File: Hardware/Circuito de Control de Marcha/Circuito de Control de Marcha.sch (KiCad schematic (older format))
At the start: 42 parts, among them Q1 IRF9540N, Q1A1 2N2219, Q2 IRF540N, Q2A1 2N2219, Q3 IRF9540N, Q3A1 2N2219, Q4 IRF540N, Q4A1 2N2219, Q5 IRF9540N, Q5A1 2N2219, Q6 IRF540N, Q6A1 2N2219, Q7 IRF9540N, Q7A1 2N2219, Q8 IRF540N, Q8A1 2N2219, U1 ULN2003

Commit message: Correxion en el control de marcha
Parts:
- removed uC_Direccion1: Screw_Terminal_01x05, Connector_Molex:Molex_KK-254_AE-6410-05A_1x05_P2.54mm_Vertical, symbol Connector:Screw_Terminal_01x05
- added uCDireccion1: Screw_Terminal_01x04, Connector_Molex:Molex_KK-254_AE-6410-04A_1x04_P2.54mm_Vertical, symbol Connector:Screw_Terminal_01x04
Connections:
- wire segments 123 -> 120
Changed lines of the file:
@@
 Wire Wire Line
 	3350 5550 4450 5550
-$Comp
-L Connector:Screw_Terminal_01x05 uC_Direccion1
-U 1 1 5E9D6D91
-P 1050 5450
-F 0 "uC_Direccion1" H 968 5775 50  0000 C CNN
-F 1 "Screw_Terminal_01x05" H 968 5776 50  0001 C CNN
-F 2 "Connector_Molex:Molex_KK-254_AE-6410-05A_1x05_P2.54mm_Vertical" H 1050 5450 50  0001 C CNN
-F 3 "~" H 1050 5450 50  0001 C CNN
-	1    1050 5450
-	-1   0    0    -1
-$EndComp
-Wire Wire Line
-	1250 5650 1450 5650
-Wire Wire Line
-	1450 5650 1450 6050
-Wire Wire Line
-	1450 6050 2950 6050
 Connection ~ 2950 6050
 $Comp
@@
 Wire Wire Line
 	5050 6050 2950 6050
+$Comp
+L Connector:Screw_Terminal_01x04 uCDireccion1
+U 1 1 5EFAC944
+P 1050 5450
+F 0 "uCDireccion1" H 968 5025 50  0000 C CNN
+F 1 "Screw_Terminal_01x04" H 968 5116 50  0000 C CNN
+F 2 "Connector_Molex:Molex_KK-254_AE-6410-04A_1x04_P2.54mm_Vertical" H 1050 5450 50  0001 C CNN
+F 3 "~" H 1050 5450 50  0001 C CNN
+	1    1050 5450
+	-1   0    0    1
+$EndComp
 $EndSCHEMATC

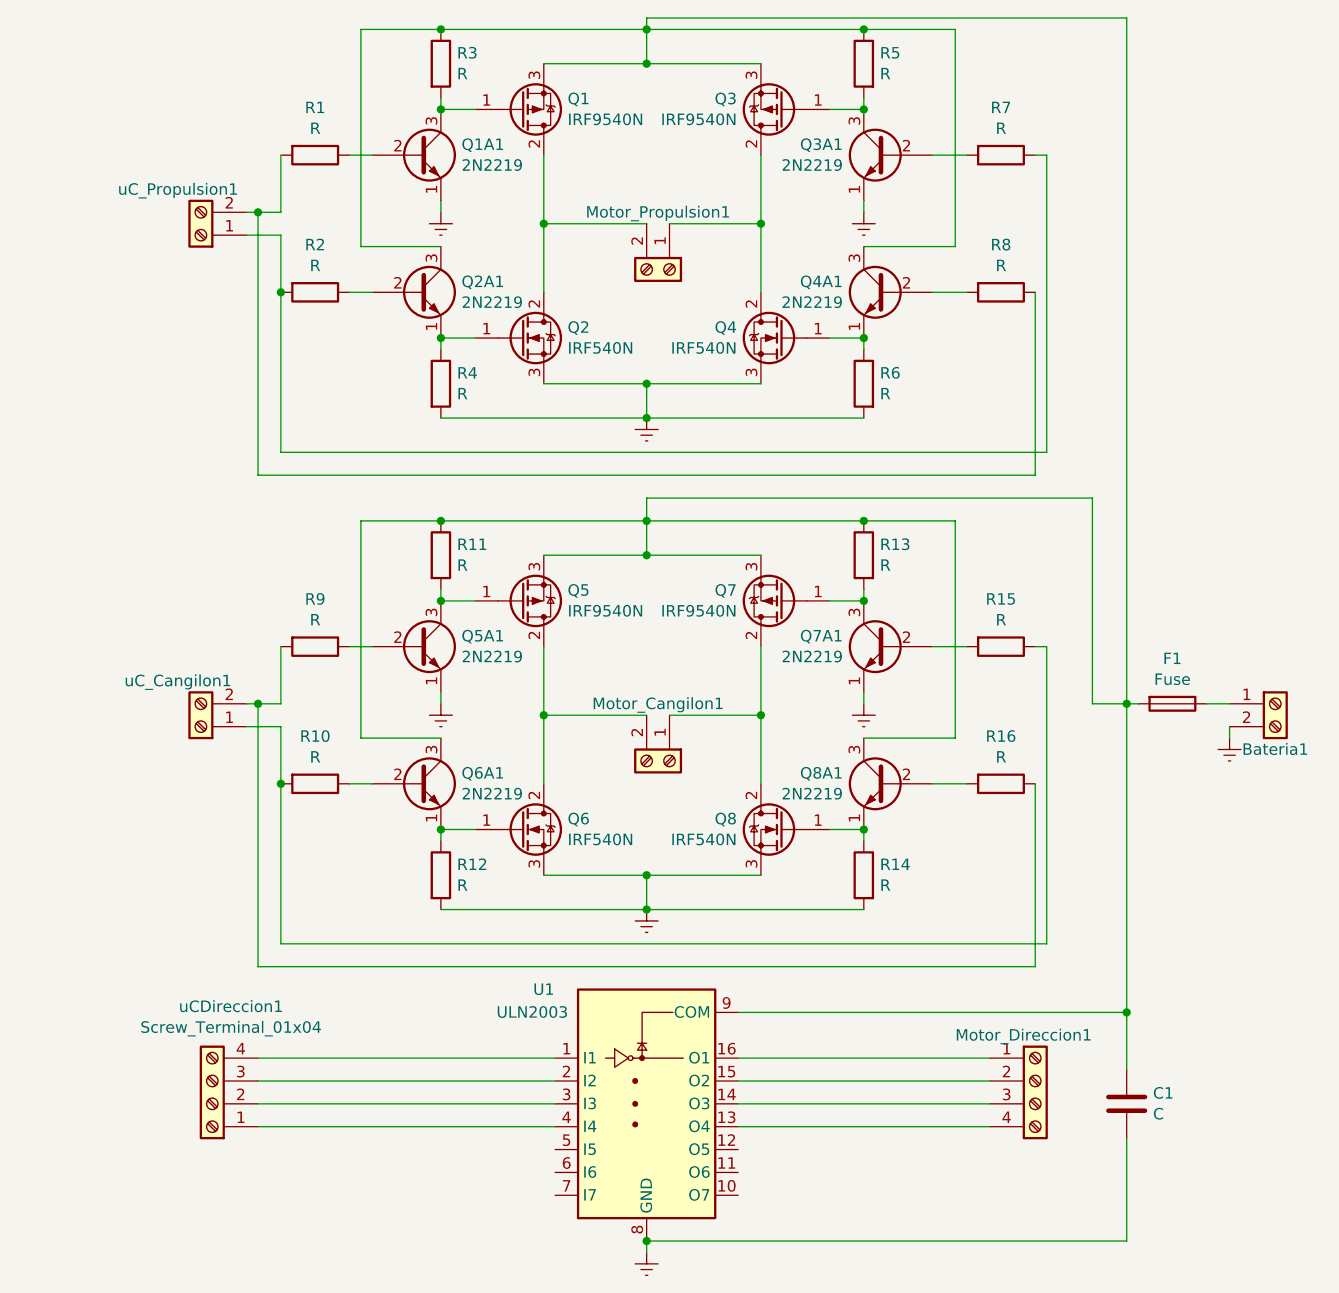
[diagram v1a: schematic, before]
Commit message: Esquematico CCM
Puse los optoacopladores en el controlador de marcha
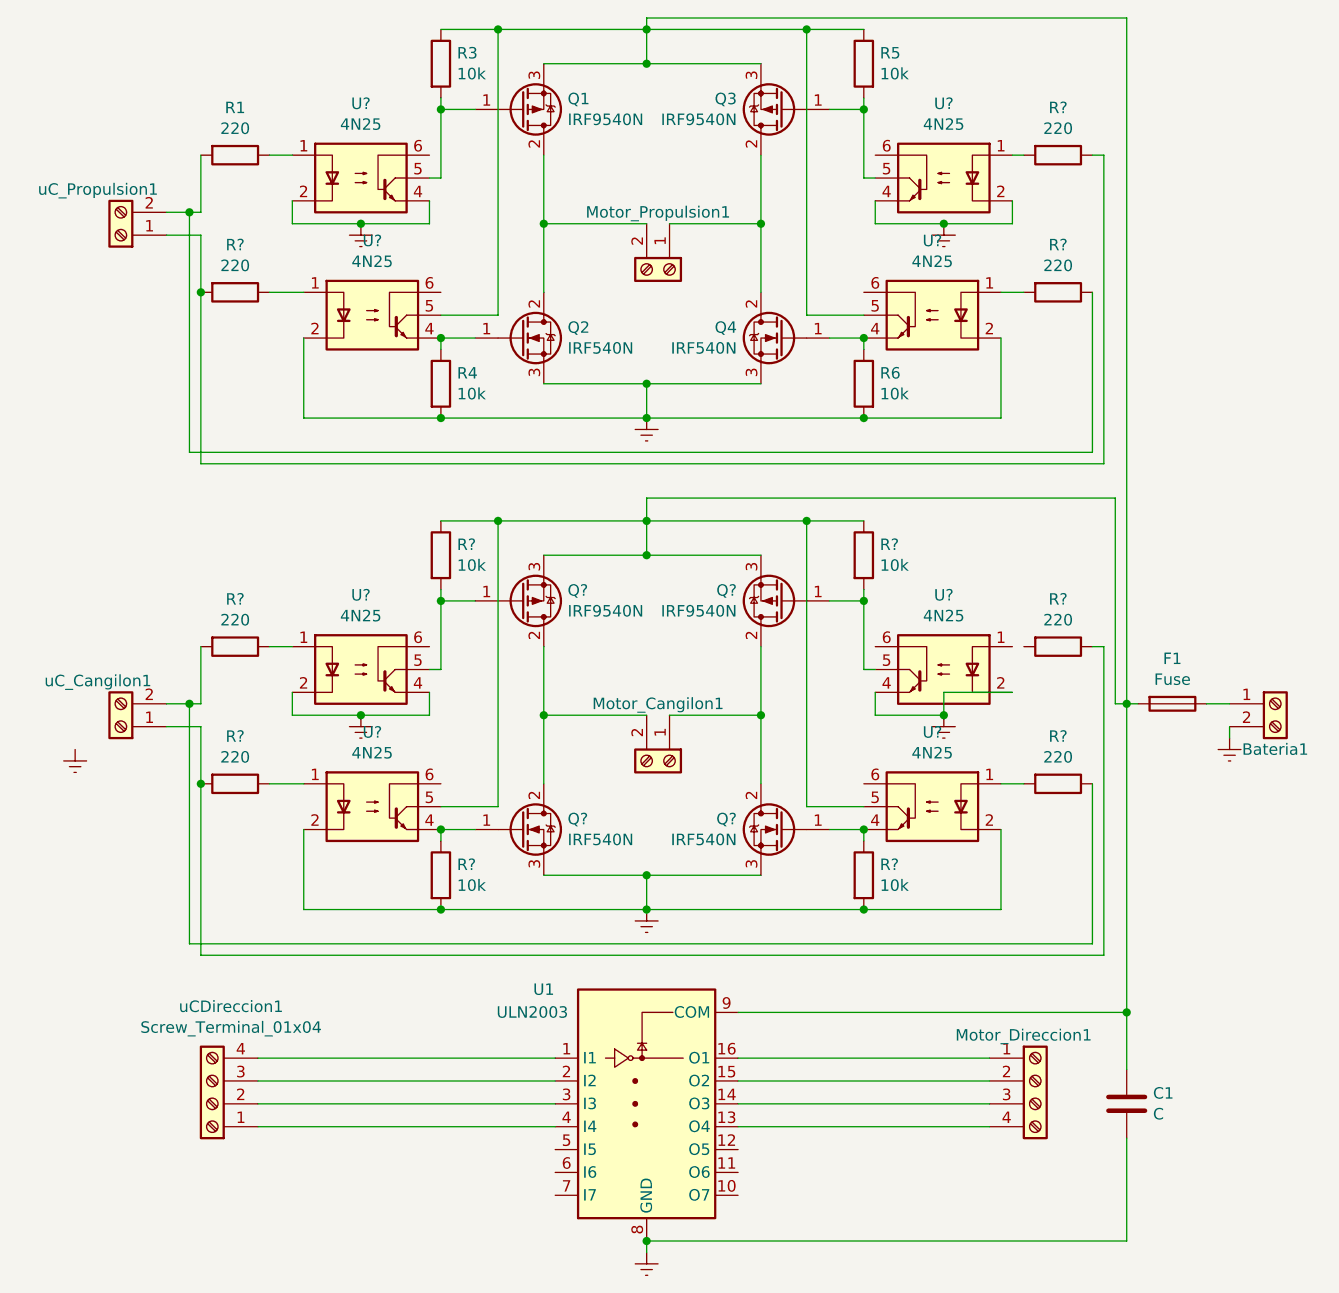
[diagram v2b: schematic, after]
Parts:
- removed Q1A1, Q2A1, Q3A1, Q4A1, Q5A1, Q6A1, Q7A1, Q8A1: 2N2219, Package_TO_SOT_THT:TO-92L_Inline_Wide, symbol Transistor_BJT:2N2219
- removed Q5, Q7: IRF9540N, Package_TO_SOT_THT:TO-220-3_Vertical, symbol Transistor_FET:IRF9540N
- removed Q6, Q8: IRF540N, Package_TO_SOT_THT:TO-220-3_Vertical, symbol Transistor_FET:IRF540N
- removed R10, R11, R12, R13, R14, R15, R16, R2, R7, R8, R9: R, Resistor_THT:R_Axial_DIN0204_L3.6mm_D1.6mm_P7.62mm_Horizontal, symbol Device:R
- added Q? (x2): IRF9540N, Package_TO_SOT_THT:TO-220-3_Vertical, symbol Transistor_FET:IRF9540N
- added Q? (x2): IRF540N, Package_TO_SOT_THT:TO-220-3_Vertical, symbol Transistor_FET:IRF540N
- added R? (x7): 220, Resistor_THT:R_Axial_DIN0204_L3.6mm_D1.6mm_P7.62mm_Horizontal, symbol Device:R
- added R? (x4): 10k, Resistor_THT:R_Axial_DIN0204_L3.6mm_D1.6mm_P7.62mm_Horizontal, symbol Device:R
- added U? (x8): 4N25, Package_DIP:DIP-6_W7.62mm, symbol Isolator:4N25
- R1: value R -> 220
- R3, R4, R5, R6: value R -> 10k
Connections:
- net Earth: now also Q?.3 (S), Q?.3 (S), R?.2, R?.2, U?.2, U?.2, U?.2, U?.2, U?.2, U?.2, U?.2, U?.2, U?.4, U?.4, U?.4, U?.4
- net at uC_Propulsion1.1 (Pin_1): now also R?.1, R?.2
- net at R1.2, uC_Propulsion1.2 (Pin_2): now also R?.1
- net at C1.1, F1.2, Q1.3 (S)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: now also Q?.3 (S), Q?.3 (S), R?.1, R?.1, U?.5, U?.5, U?.5, U?.5
- net at Q1.1 (G), R3.2: now also U?.5
- net at Q2.1 (G), R4.1: now also U?.4
- net at R1.1: now also U?.1
- net at Q3.1 (G), R5.2: now also U?.5
- net at Q4.1 (G), R6.1: now also U?.4
- net at uC_Cangilon1.1 (Pin_1): now also R?.1, R?.2
- net at uC_Cangilon1.2 (Pin_2): now also R?.1, R?.2
- net at Motor_Cangilon1.2 (Pin_2): now also Q?.2 (D), Q?.2 (D)
- net at Motor_Cangilon1.1 (Pin_1): now also Q?.2 (D), Q?.2 (D)
- new net: R?.1, U?.1 (x3)
- new net: R?.2, U?.1 (x3)
- new net: Q?.1 (G), R?.2, U?.5 (x2)
- new net: Q?.1 (G), R?.1, U?.4 (x2)
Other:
- moved on the sheet: R1, uC_Cangilon1, uC_Propulsion1

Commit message: PCB control de marcha
Intente hacer el PCB pero me queda una conexion de los púentes H
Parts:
- gave numbers to parts that had none: 23
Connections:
- net at U9.1: now also R15.2
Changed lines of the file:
@@
 $EndComp
 $Comp
-L Isolator:4N25 U?
+L Isolator:4N25 U2
 U 1 1 5F002069
 P 1700 1400
-F 0 "U?" H 1700 1725 50  0000 C CNN
+F 0 "U2" H 1700 1725 50  0000 C CNN
 F 1 "4N25" H 1700 1634 50  0000 C CNN
 F 2 "Package_DIP:DIP-6_W7.62mm" H 1500 1200 50  0001 L CIN
@@
 Connection ~ 1700 1600
 $Comp
-L Isolator:4N25 U?
+L Isolator:4N25 U4
 U 1 1 5F020A68
 P 1750 2000
-F 0 "U?" H 1750 2325 50  0000 C CNN
+F 0 "U4" H 1750 2325 50  0000 C CNN
 F 1 "4N25" H 1750 2234 50  0000 C CNN
 F 2 "Package_DIP:DIP-6_W7.62mm" H 1550 1800 50  0001 L CIN
@@
 Connection ~ 2050 2450
 $Comp
-L Isolator:4N25 U?
+L Isolator:4N25 U6
 U 1 1 5F02FF87
 P 4200 2000
-F 0 "U?" H 4200 2325 50  0000 C CNN
+F 0 "U6" H 4200 2325 50  0000 C CNN
 F 1 "4N25" H 4200 2234 50  0000 C CNN
 F 2 "Package_DIP:DIP-6_W7.62mm" H 4000 1800 50  0001 L CIN
@@
 Connection ~ 3900 2100
 $Comp
-L Isolator:4N25 U?
+L Isolator:4N25 U8
 U 1 1 5F033177
 P 4250 1400
-F 0 "U?" H 4250 1725 50  0000 C CNN
+F 0 "U8" H 4250 1725 50  0000 C CNN
 F 1 "4N25" H 4250 1634 50  0000 C CNN
 F 2 "Package_DIP:DIP-6_W7.62mm" H 4050 1200 50  0001 L CIN
@@
 	4950 2650 1000 2650
 $Comp
-L Transistor_FET:IRF9540N Q?
+L Transistor_FET:IRF9540N Q5
 U 1 1 5F05B32E
 P 2400 3250
-F 0 "Q?" H 2604 3204 50  0000 L CNN
+F 0 "Q5" H 2604 3204 50  0000 L CNN
 F 1 "IRF9540N" H 2604 3295 50  0000 L CNN
 F 2 "Package_TO_SOT_THT:TO-220-3_Vertical" H 2600 3175 50  0001 L CIN
@@
 $EndComp
 $Comp
-L Transistor_FET:IRF9540N Q?
+L Transistor_FET:IRF9540N Q7
 U 1 1 5F05BBDD
 P 3550 3250
-F 0 "Q?" H 3755 3204 50  0000 L CNN
+F 0 "Q7" H 3755 3204 50  0000 L CNN
 F 1 "IRF9540N" H 3755 3295 50  0000 L CNN
 F 2 "Package_TO_SOT_THT:TO-220-3_Vertical" H 3750 3175 50  0001 L CIN
@@
 $EndComp
 $Comp
-L Transistor_FET:IRF540N Q?
+L Transistor_FET:IRF540N Q6
 U 1 1 5F05C27A
 P 2400 4250
-F 0 "Q?" H 2604 4296 50  0000 L CNN
+F 0 "Q6" H 2604 4296 50  0000 L CNN
 F 1 "IRF540N" H 2604 4205 50  0000 L CNN
 F 2 "Package_TO_SOT_THT:TO-220-3_Vertical" H 2650 4175 50  0001 L CIN
@@
 $EndComp
 $Comp
-L Transistor_FET:IRF540N Q?
+L Transistor_FET:IRF540N Q8
 U 1 1 5F05CF57
 P 3550 4250
-F 0 "Q?" H 3755 4296 50  0000 L CNN
+F 0 "Q8" H 3755 4296 50  0000 L CNN
 F 1 "IRF540N" H 3755 4205 50  0000 L CNN
 F 2 "Package_TO_SOT_THT:TO-220-3_Vertical" H 3800 4175 50  0001 L CIN
@@
 	1000 1650 1000 1900
 $Comp
-L Device:R R?
+L Device:R R2
 U 1 1 5F063F20
 P 1150 1900
-F 0 "R?" V 943 1900 50  0000 C CNN
+F 0 "R2" V 943 1900 50  0000 C CNN
 F 1 "220" V 1034 1900 50  0000 C CNN
 F 2 "Resistor_THT:R_Axial_DIN0204_L3.6mm_D1.6mm_P7.62mm_Horizontal" V 1080 1900 50  0001 C CNN
@@
 	1000 1900 1000 2650
 $Comp
-L Device:R R?
+L Device:R R14
 U 1 1 5F0641E7
 P 4750 1900
-F 0 "R?" V 4543 1900 50  0000 C CNN
+F 0 "R14" V 4543 1900 50  0000 C CNN
 F 1 "220" V 4634 1900 50  0000 C CNN
 F 2 "Resistor_THT:R_Axial_DIN0204_L3.6mm_D1.6mm_P7.62mm_Horizontal" V 4680 1900 50  0001 C CNN
@@
 $EndComp
 $Comp
-L Device:R R?
+L Device:R R13
 U 1 1 5F0646E3
 P 4750 1300
-F 0 "R?" V 4543 1300 50  0000 C CNN
+F 0 "R13" V 4543 1300 50  0000 C CNN
 F 1 "220" V 4634 1300 50  0000 C CNN
 F 2 "Resistor_THT:R_Axial_DIN0204_L3.6mm_D1.6mm_P7.62mm_Horizontal" V 4680 1300 50  0001 C CNN
@@
 	850  3700 950  3700
 $Comp
-L Isolator:4N25 U?
+L Isolator:4N25 U5
 U 1 1 5F06CB3C
 P 1750 4150
-F 0 "U?" H 1750 4475 50  0000 C CNN
+F 0 "U5" H 1750 4475 50  0000 C CNN
 F 1 "4N25" H 1750 4384 50  0000 C CNN
 F 2 "Package_DIP:DIP-6_W7.62mm" H 1550 3950 50  0001 L CIN
@@
 Connection ~ 2050 4250
 $Comp
-L Isolator:4N25 U?
+L Isolator:4N25 U3
 U 1 1 5F0726D9
 P 1700 3550
-F 0 "U?" H 1700 3875 50  0000 C CNN
+F 0 "U3" H 1700 3875 50  0000 C CNN
 F 1 "4N25" H 1700 3784 50  0000 C CNN
 F 2 "Package_DIP:DIP-6_W7.62mm" H 1500 3350 50  0001 L CIN
@@
 $EndComp
 $Comp
-L Isolator:4N25 U?
+L Isolator:4N25 U7
 U 1 1 5F0735D6
 P 4200 4150
-F 0 "U?" H 4200 4475 50  0000 C CNN
+F 0 "U7" H 4200 4475 50  0000 C CNN
 F 1 "4N25" H 4200 4384 50  0000 C CNN
 F 2 "Package_DIP:DIP-6_W7.62mm" H 4000 3950 50  0001 L CIN
@@
 Connection ~ 3900 4250
 $Comp
-L Isolator:4N25 U?
+L Isolator:4N25 U9
 U 1 1 5F07448D
 P 4250 3550
-F 0 "U?" H 4250 3875 50  0000 C CNN
+F 0 "U9" H 4250 3875 50  0000 C CNN
 F 1 "4N25" H 4250 3784 50  0000 C CNN
 F 2 "Package_DIP:DIP-6_W7.62mm" H 4050 3350 50  0001 L CIN
@@
 $EndComp
 $Comp
-L power:Earth #PWR?
+L power:Earth #PWR0105
 U 1 1 5F075575
 P 4250 3750
-F 0 "#PWR?" H 4250 3500 50  0001 C CNN
+F 0 "#PWR0105" H 4250 3500 50  0001 C CNN
 F 1 "Earth" H 4250 3600 50  0001 C CNN
 F 2 "" H 4250 3750 50  0001 C CNN
@@
 $EndComp
 $Comp
-L Device:R R?
+L Device:R R16
 U 1 1 5F07592F
 P 4750 4050
-F 0 "R?" V 4543 4050 50  0000 C CNN
+F 0 "R16" V 4543 4050 50  0000 C CNN
 F 1 "220" V 4634 4050 50  0000 C CNN
 F 2 "Resistor_THT:R_Axial_DIN0204_L3.6mm_D1.6mm_P7.62mm_Horizontal" V 4680 4050 50  0001 C CNN
@@
 $EndComp
 $Comp
-L Device:R R?
+L Device:R R15
 U 1 1 5F075D82
 P 4750 3450
-F 0 "R?" V 4543 3450 50  0000 C CNN
+F 0 "R15" V 4543 3450 50  0000 C CNN
 F 1 "220" V 4634 3450 50  0000 C CNN
 F 2 "Resistor_THT:R_Axial_DIN0204_L3.6mm_D1.6mm_P7.62mm_Horizontal" V 4680 3450 50  0001 C CNN
@@
 	2950 2800 5000 2800
 $Comp
-L Device:R R?
+L Device:R R7
 U 1 1 5F07AAF0
 P 1150 3450
-F 0 "R?" V 943 3450 50  0000 C CNN
+F 0 "R7" V 943 3450 50  0000 C CNN
 F 1 "220" V 1034 3450 50  0000 C CNN
 F 2 "Resistor_THT:R_Axial_DIN0204_L3.6mm_D1.6mm_P7.62mm_Horizontal" V 1080 3450 50  0001 C CNN
@@
 $EndComp
 $Comp
-L Device:R R?
+L Device:R R8
 U 1 1 5F07B007
 P 1150 4050
-F 0 "R?" V 943 4050 50  0000 C CNN
+F 0 "R8" V 943 4050 50  0000 C CNN
 F 1 "220" V 1034 4050 50  0000 C CNN
 F 2 "Resistor_THT:R_Axial_DIN0204_L3.6mm_D1.6mm_P7.62mm_Horizontal" V 1080 4050 50  0001 C CNN
@@
 	1300 4050 1450 4050
 $Comp
-L power:Earth #PWR?
+L power:Earth #PWR0109
 U 1 1 5F083A08
 P 1700 3750
-F 0 "#PWR?" H 1700 3500 50  0001 C CNN
+F 0 "#PWR0109" H 1700 3500 50  0001 C CNN
 F 1 "Earth" H 1700 3600 50  0001 C CNN
 F 2 "" H 1700 3750 50  0001 C CNN
@@
 	2950 4600 3900 4600
 $Comp
-L Device:R R?
+L Device:R R9
 U 1 1 5F0CA0D4
 P 2050 3050
-F 0 "R?" H 2120 3096 50  0000 L CNN
+F 0 "R9" H 2120 3096 50  0000 L CNN
 F 1 "10k" H 2120 3005 50  0000 L CNN
 F 2 "Resistor_THT:R_Axial_DIN0204_L3.6mm_D1.6mm_P7.62mm_Horizontal" V 1980 3050 50  0001 C CNN
@@
 $EndComp
 $Comp
-L Device:R R?
+L Device:R R10
 U 1 1 5F0CA4D1
 P 2050 4450
-F 0 "R?" H 2120 4496 50  0000 L CNN
+F 0 "R10" H 2120 4496 50  0000 L CNN
 F 1 "10k" H 2120 4405 50  0000 L CNN
 F 2 "Resistor_THT:R_Axial_DIN0204_L3.6mm_D1.6mm_P7.62mm_Horizontal" V 1980 4450 50  0001 C CNN
@@
 	2050 4600 2950 4600
 $Comp
-L Device:R R?
+L Device:R R11
 U 1 1 5F0CAFB0
 P 3900 3050
-F 0 "R?" H 3970 3096 50  0000 L CNN
+F 0 "R11" H 3970 3096 50  0000 L CNN
 F 1 "10k" H 3970 3005 50  0000 L CNN
 F 2 "Resistor_THT:R_Axial_DIN0204_L3.6mm_D1.6mm_P7.62mm_Horizontal" V 3830 3050 50  0001 C CNN
@@
 $EndComp
 $Comp
-L Device:R R?
+L Device:R R12
 U 1 1 5F0CB34B
 P 3900 4450
-F 0 "R?" H 3970 4496 50  0000 L CNN
+F 0 "R12" H 3970 4496 50  0000 L CNN
 F 1 "10k" H 3970 4405 50  0000 L CNN
 F 2 "Resistor_THT:R_Axial_DIN0204_L3.6mm_D1.6mm_P7.62mm_Horizontal" V 3830 4450 50  0001 C CNN
@@
 Wire Wire Line
 	2050 4150 2300 4150
+Wire Wire Line
+	4600 3450 4550 3450
 $EndSCHEMATC
